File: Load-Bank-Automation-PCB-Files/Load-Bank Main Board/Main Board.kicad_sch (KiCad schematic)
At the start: 4 parts

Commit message: Schematic for review
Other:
- removed sheet MOSFET Boards
- note added: "- The soft start time for the eFuse is 141 ms, while the soft start of the buck is 25 ms, would that cause an issue? - The Buck Was Simulated/Created Using Webench, it would be Awsome if you just skimmed over it. I double checked some of the values as well. -"
- note removed: "MOSFET Boards"
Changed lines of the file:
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@@
 	(paper "A4")
-	(rectangle
-		(start 85.09 19.05)
-		(end 133.35 60.96)
-		(stroke
-			(width 0)
-			(type dot)
-		)
-		(fill
-			(type none)
-		)
-	)
 	(rectangle
 		(start 15.24 15.24)
@@
 		)
 	)
-	(text "MOSFET Boards"
-		(exclude_from_sim no)
-		(at 96.266 17.018 0)
+	(text "- The soft start time for the eFuse is 141 ms, while the soft start \nof the buck is 25 ms, would that cause an issue?\n- The Buck Was Simulated/Created Using Webench, it would be \nAwsome if you just skimmed over it. I double checked some of the \nvalues as well.\n-"
+		(exclude_from_sim no)
+		(at 27.94 70.866 0)
 		(effects
 			(font
-				(size 1.778 1.778)
-				(thickness 0.3556)
-				(bold yes)
-			)
+				(size 1.27 1.27)
+			)
+			(justify left)
 		)
 	)
@@
 				)
 			)
-		)
-	)
-	(sheet
-		(at 90.17 24.13)
-		(size 39.37 31.75)
-		(exclude_from_sim no)
-		(in_bom yes)
-		(on_board yes)
-		(dnp no)
-		(fields_autoplaced yes)
-		(stroke
-			(width 0.1524)
-			(type solid)
-		)
-		(fill
-			(color 0 0 0 0.0000)
-		)
-		(property "Sheetname" "MOSFET Boards"
-			(at 90.17 23.4184 0)
-			(effects
-				(font
-					(size 1.27 1.27)
-				)
-				(justify left bottom)
-			)
-		)
-		(property "Sheetfile" "MOSFET Boards.kicad_sch"
-			(at 90.17 56.4646 0)
-			(effects
-				(font
-					(size 1.27 1.27)
-				)
-				(justify left top)
-			)
-		)
-		(instances
-			(project "Main Board"
-				(path "/c82c4769-33eb-46b7-8d07-39045014a3da"
-					(page "9")
-				)
-			)

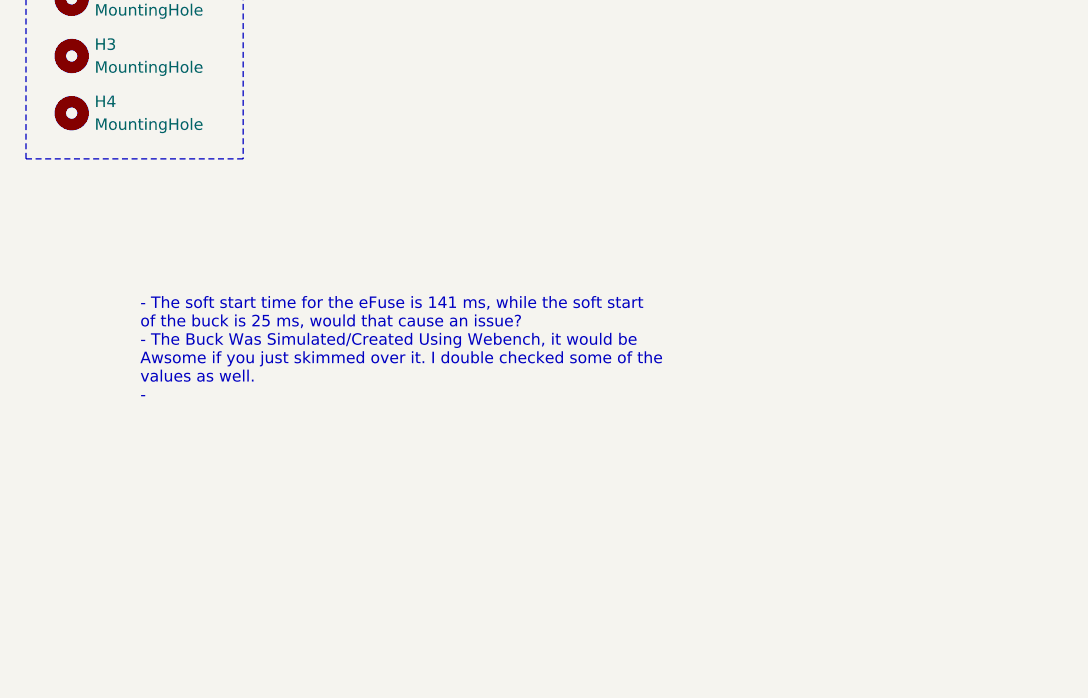
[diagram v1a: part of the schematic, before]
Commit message: Almost completed MOSFET board component selection
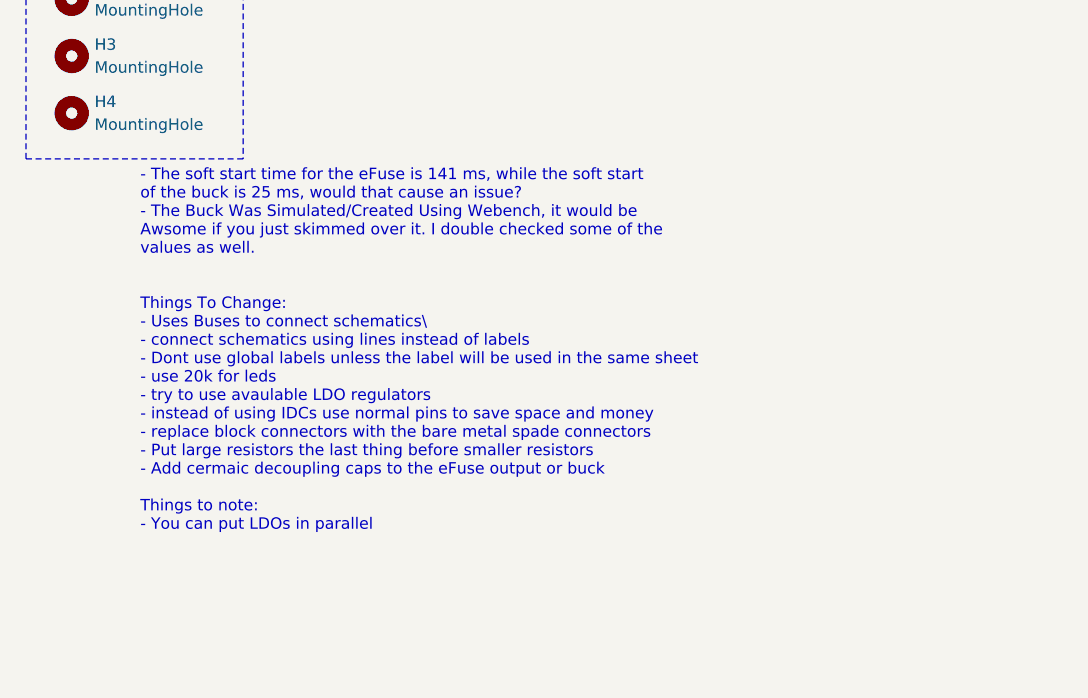
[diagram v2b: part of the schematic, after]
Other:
- note added: "- The soft start time for the eFuse is 141 ms, while the soft start of the buck is 25 ms, would that cause an issue? - The Buck Was Simulated/Created Using Webench, it would be Awsome if you just skimmed over it. I double checked some of the values as well. Things To Change: - Uses Buses to connect schematics\ - connect schematics using lines instead of labels - Dont use global labels unless the 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"
- note removed: "- The soft start time for the eFuse is 141 ms, while the soft start of the buck is 25 ms, would that cause an issue? - The Buck Was Simulated/Created Using Webench, it would be Awsome if you just skimmed over it. I double checked some of the values as well. -"
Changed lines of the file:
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@@
 		)
 	)
-	(text "- The soft start time for the eFuse is 141 ms, while the soft start \nof the buck is 25 ms, would that cause an issue?\n- The Buck Was Simulated/Created Using Webench, it would be \nAwsome if you just skimmed over it. I double checked some of the \nvalues as well.\n-"
+	(text "- The soft start time for the eFuse is 141 ms, while the soft start \nof the buck is 25 ms, would that cause an issue?\n- The Buck Was Simulated/Created Using Webench, it would be \nAwsome if you just skimmed over it. I double checked some of the \nvalues as well.\n\n\nThings To Change:\n- Uses Buses to connect schematics\\\n- connect schematics using lines instead of labels\n- Dont use global labels unless the label will be used in the same sheet\n- use 20k for leds\n- try to use avaulable LDO regulators\n- instead of using IDCs use normal pins to save space and money\n- replace block connectors with the bare metal spade connectors\n- Put large resistors the last thing before smaller resistors \n- Add cermaic decoupling caps to the eFuse output or buck\n\nThings to note:\n- You can put LDOs in parallel"
 		(exclude_from_sim no)
 		(at 27.94 70.866 0)
@@
 		)
 		(fill
-			(color 0 0 0 0.0000)
+			(color 255 229 191 1.0000)
 		)
 		(property "Sheetname" "Main_Power"
